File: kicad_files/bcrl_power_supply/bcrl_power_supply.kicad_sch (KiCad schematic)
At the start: 7 parts, among them J1 OSTVN02A150, J2 OSTVN02A150, J3 OSTVN02A150, J4 OSTVN02A150, J5 OSTVN02A150, J6 OSTVN02A150, J7 OSTVN02A150

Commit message: ...
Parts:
- added CJ2, PJ1: Conn_01x10, Connector_PinSocket_2.54mm:PinSocket_1x10_P2.54mm_Vertical, symbol Connector_Generic:Conn_01x10
- added P1: Conn_01x10, Connector_PinSocket_1.27mm:PinSocket_1x10_P1.27mm_Vertical, symbol Connector_Generic:Conn_01x10
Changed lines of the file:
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@@
+    )
+  )
+  (symbol (lib_id "Connector_Generic:Conn_01x10") (at 66.04 171.45 0) (unit 1)
+    (in_bom yes) (on_board yes) (dnp no) (fields_autoplaced)
+    (property "Reference" "P1" (at 68.58 171.45 0)
+      (effects (font (size 1.27 1.27)) (justify left))
+    )
+    (property "Value" "Conn_01x10" (at 68.58 173.99 0)
+      (effects (font (size 1.27 1.27)) (justify left))
+    )
+    (property "Footprint" "Connector_PinSocket_1.27mm:PinSocket_1x10_P1.27mm_Vertical" (at 66.04 171.45 0)
+      (effects (font (size 1.27 1.27)) hide)
+    )
+    (property "Datasheet" "~" (at 66.04 171.45 0)
+      (effects (font (size 1.27 1.27)) hide)
+    )
+    (pin "6")
+    (pin "9")
+    (pin "8")
+    (pin "5")
+    (pin "4")
+    (pin "3")
+    (pin "2")
+    (pin "10")
+    (pin "1")
+    (pin "7")
+    (instances
+      (project "bcrl_power_supply"
+        (path "/77f0f57c-9586-4625-9281-fa8cbd8015db"
+          (reference "P1") (unit 1)
+        )
+      )
     )
   )
@@
     )
   )
-  (symbol (lib_id "power:GND") (at 60.96 24.13 0) (unit 1)
-    (in_bom yes) (on_board yes) (dnp no) (fields_autoplaced)
-    (property "Reference" "#PWR02" (at 60.96 30.48 0)
-      (effects (font (size 1.27 1.27)) hide)
-    )
-    (property "Value" "GND" (at 60.96 29.21 0)
+  (symbol (lib_id "power:GND") (at 68.58 27.94 0) (unit 1)
+    (in_bom yes) (on_board yes) (dnp no) (fields_autoplaced)
+    (property "Reference" "#PWR02" (at 68.58 34.29 0)
+      (effects (font (size 1.27 1.27)) hide)
+    )
+    (property "Value" "GND" (at 68.58 33.02 0)
       (effects (font (size 1.27 1.27)))
     )
-    (property "Footprint" "" (at 60.96 24.13 0)
-      (effects (font (size 1.27 1.27)) hide)
-    )
-    (property "Datasheet" "" (at 60.96 24.13 0)
+    (property "Footprint" "" (at 68.58 27.94 0)
+      (effects (font (size 1.27 1.27)) hide)
+    )
+    (property "Datasheet" "" (at 68.58 27.94 0)
       (effects (font (size 1.27 1.27)) hide)
     )
@@
     )
   )
+  (symbol (lib_id "Connector_Generic:Conn_01x10") (at 67.31 128.27 0) (unit 1)
+    (in_bom yes) (on_board yes) (dnp no) (fields_autoplaced)
+    (property "Reference" "PJ1" (at 69.85 128.27 0)
+      (effects (font (size 1.27 1.27)) (justify left))
+    )
+    (property "Value" "Conn_01x10" (at 69.85 130.81 0)
+      (effects (font (size 1.27 1.27)) (justify left))
+    )
+    (property "Footprint" "Connector_PinSocket_2.54mm:PinSocket_1x10_P2.54mm_Vertical" (at 67.31 128.27 0)
+      (effects (font (size 1.27 1.27)) hide)
+    )
+    (property "Datasheet" "~" (at 67.31 128.27 0)
+      (effects (font (size 1.27 1.27)) hide)
+    )
+    (pin "6")
+    (pin "9")
+    (pin "8")
+    (pin "5")
+    (pin "4")
+    (pin "3")
+    (pin "2")
+    (pin "10")
+    (pin "1")
+    (pin "7")
+    (instances
+      (project "bcrl_power_supply"
+        (path "/77f0f57c-9586-4625-9281-fa8cbd8015db"
+          (reference "PJ1") (unit 1)
+        )
+      )
+    )
+  )
   (symbol (lib_id "2024-02-14_22-22-09:OSTVN02A150") (at 115.57 144.78 0) (unit 1)
     (in_bom yes) (on_board yes) (dnp no) (fields_autoplaced)
@@
         )
       )
+    )
+  )
+  (symbol (lib_id "Connector_Generic:Conn_01x10") (at 67.31 100.33 0) (unit 1)
+    (in_bom yes) (on_board yes) (dnp no) (fields_autoplaced)
+    (property "Reference" "CJ2" (at 69.85 100.33 0)
+      (effects (font (size 1.27 1.27)) (justify left))
+    )
+    (property "Value" "Conn_01x10" (at 69.85 102.87 0)
+      (effects (font (size 1.27 1.27)) (justify left))
+    )
+    (property "Footprint" "Connector_PinSocket_2.54mm:PinSocket_1x10_P2.54mm_Vertical" (at 67.31 100.33 0)
+      (effects (font (size 1.27 1.27)) hide)
+    )
+    (property "Datasheet" "~" (at 67.31 100.33 0)
+      (effects (font (size 1.27 1.27)) hide)
+    )
+    (pin "6")
+    (pin "9")
+    (pin "8")
+    (pin "5")
+    (pin "4")
+    (pin "3")
+    (pin "2")
+    (pin "10")
+    (pin "1")
+    (pin "7")
+    (instances
+      (project "bcrl_power_supply"
+        (path "/77f0f57c-9586-4625-9281-fa8cbd8015db"
+          (reference "CJ2") (unit 1)
+        )
+      )

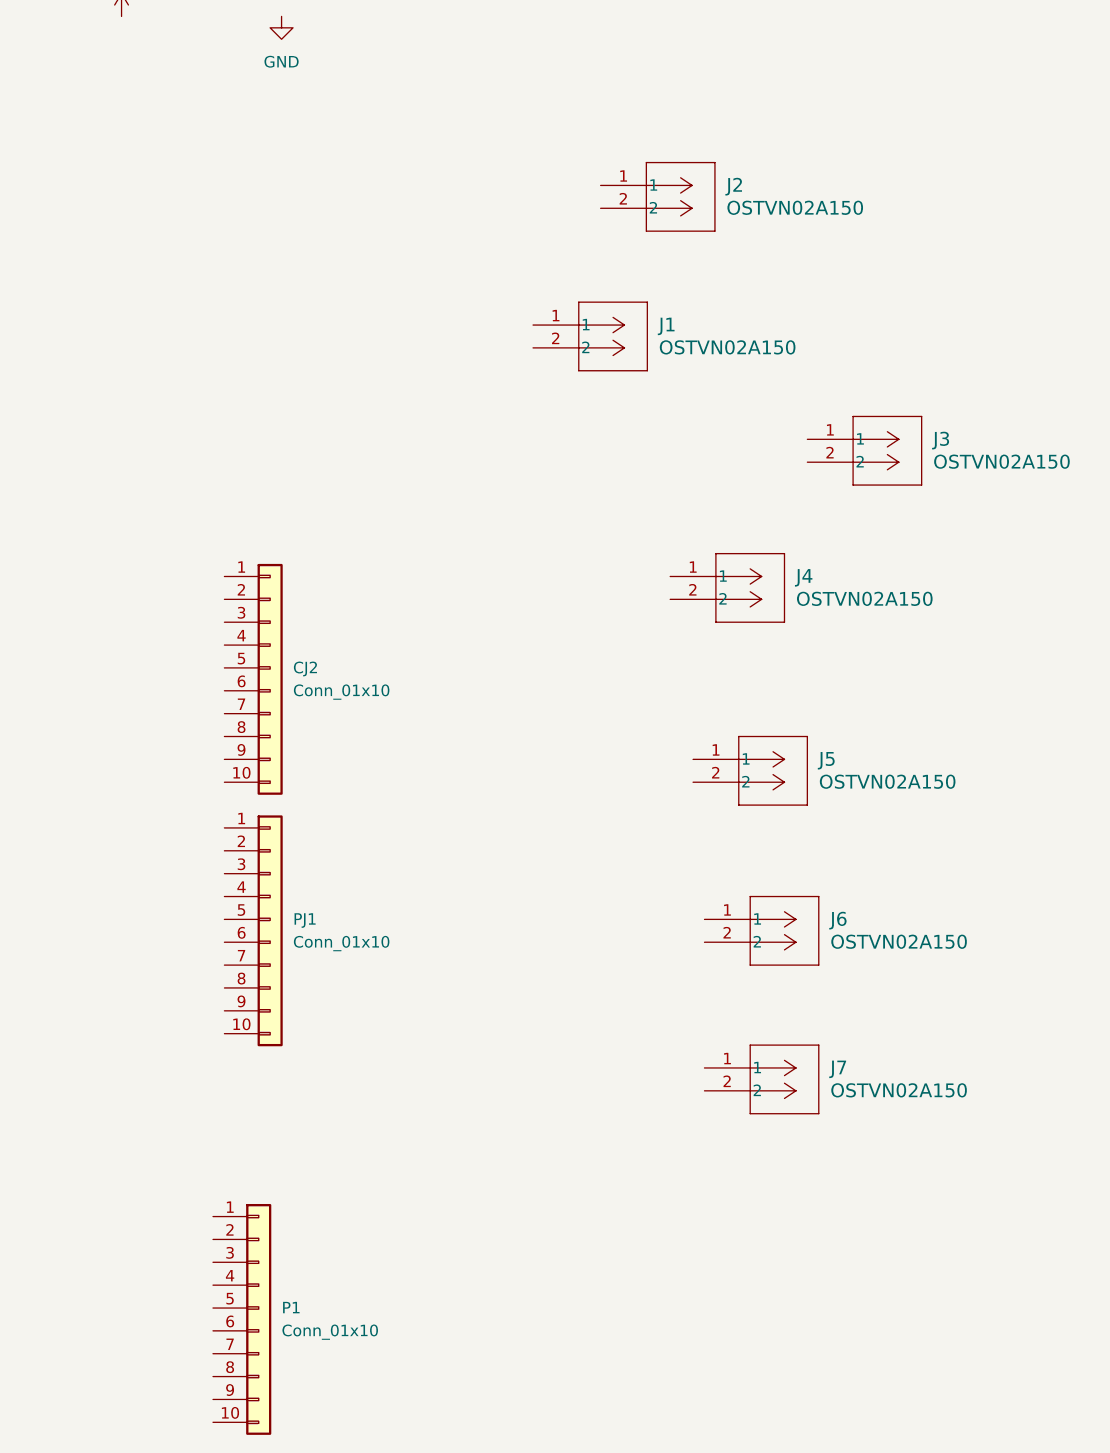
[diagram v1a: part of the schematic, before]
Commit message: added components
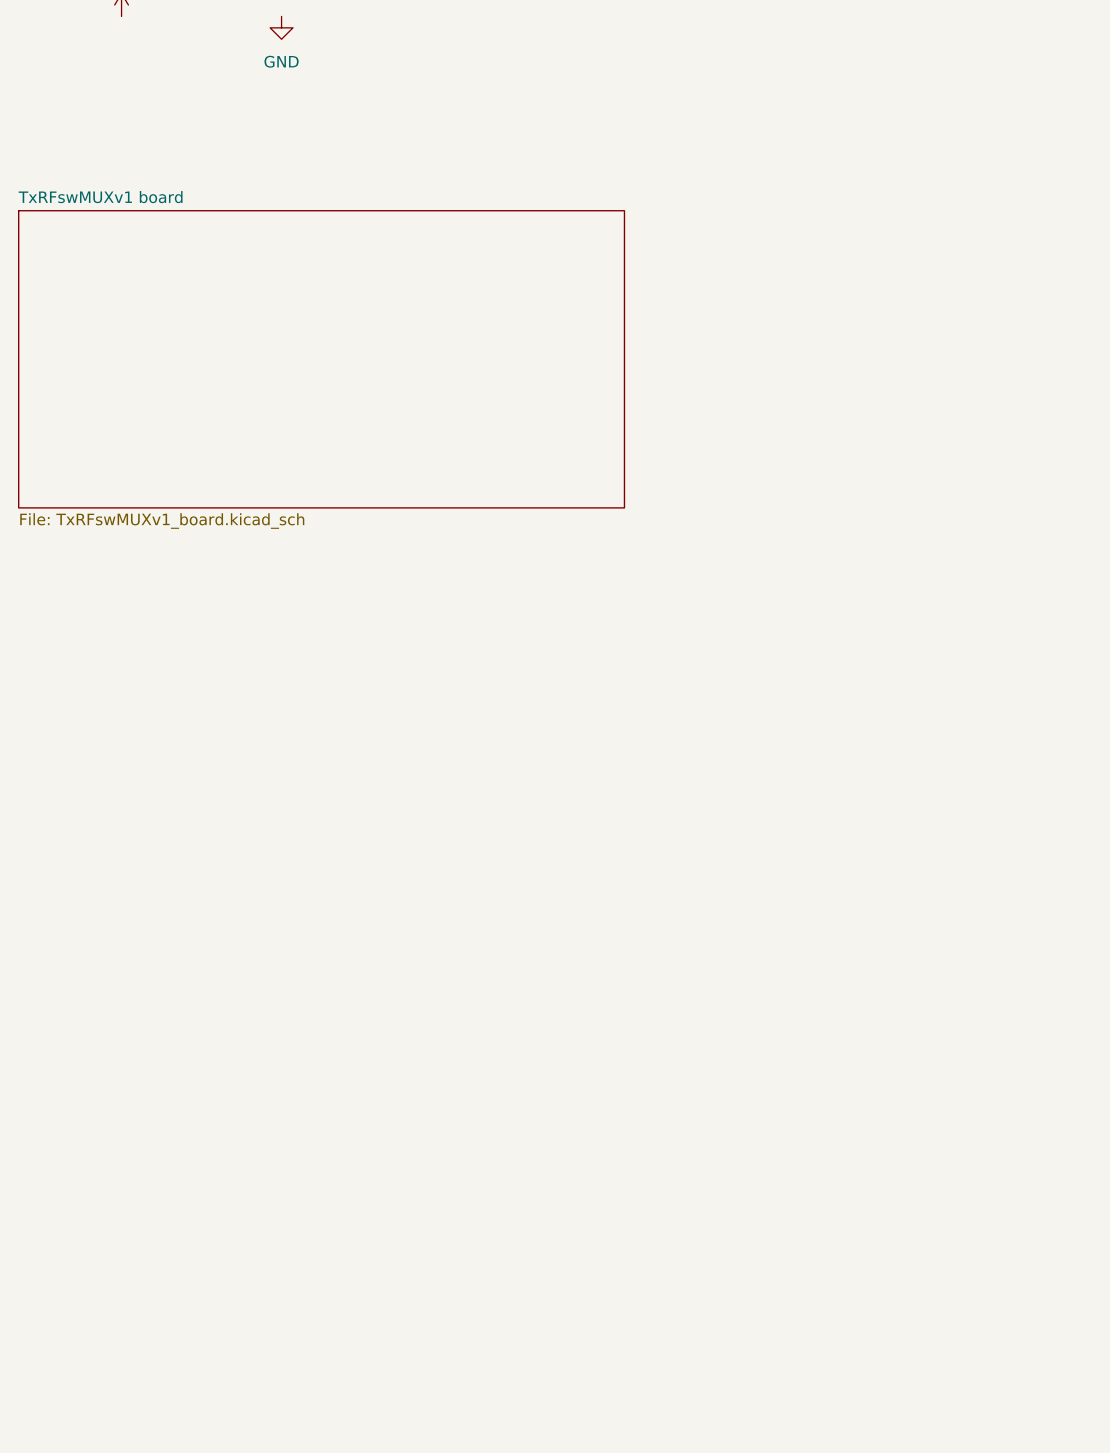
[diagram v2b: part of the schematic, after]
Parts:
- removed CJ2, PJ1: Conn_01x10, Connector_PinSocket_2.54mm:PinSocket_1x10_P2.54mm_Vertical, symbol Connector_Generic:Conn_01x10
- removed J1, J2, J3, J4, J5, J6, J7: OSTVN02A150, screw_terminal:CONN_OSTVN02A150_OST, symbol 2024-02-14_22-22-09:OSTVN02A150
- removed P1: Conn_01x10, Connector_PinSocket_1.27mm:PinSocket_1x10_P1.27mm_Vertical, symbol Connector_Generic:Conn_01x10
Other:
- added sheet TxRFswMUXv1 board (TxRFswMUXv1_board.kicad_sch)

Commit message: added decoupling
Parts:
- added J10, J12: OSTVN02A150, symbol BCRL_power_supply:OSTVN02A150
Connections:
- net +48V: now also J10.1, J12.1
- net GND: now also J10.2, J12.2
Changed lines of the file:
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@@
 (kicad_sch (version 20230121) (generator eeschema)
   (paper "A4")
-  (symbol (lib_id "power:+48V") (at 50.8 27.94 0) (unit 1)
+  (wire (pts (xy 30.48 34.29) (xy 39.37 34.29))
+    (stroke (width 0) (type default))
+  )
+  (wire (pts (xy 30.48 24.13) (xy 39.37 24.13))
+    (stroke (width 0) (type default))
+  )
+  (wire (pts (xy 30.48 36.83) (xy 39.37 36.83))
+    (stroke (width 0) (type default))
+  )
+  (wire (pts (xy 30.48 26.67) (xy 39.37 26.67))
+    (stroke (width 0) (type default))
+  )
+  (symbol (lib_id "BCRL_power_supply:OSTVN02A150") (at 39.37 34.29 0) (unit 1)
     (in_bom yes) (on_board yes) (dnp no) (fields_autoplaced)
-    (property "Reference" "#PWR01" (at 50.8 31.75 0)
+    (property "Reference" "J10" (at 53.34 34.29 0)
+      (effects (font (size 1.524 1.524)) (justify left))
+    )
+    (property "Value" "OSTVN02A150" (at 53.34 36.83 0)
+      (effects (font (size 1.524 1.524)) (justify left))
+    )
+    (property "Footprint" "" (at 29.21 29.21 0)
+      (effects (font (size 1.27 1.27) italic) hide)
+    )
+    (property "Datasheet" "" (at 33.02 31.75 0)
+      (effects (font (size 1.27 1.27) italic) hide)
+    )
+    (pin "1")
+    (pin "2")
+    (instances
+      (project "bcrl_power_supply"
+        (path "/77f0f57c-9586-4625-9281-fa8cbd8015db"
+          (reference "J10") (unit 1)
+        )
+      )
+    )
+  )
+  (symbol (lib_id "power:+48V") (at 30.48 24.13 90) (unit 1)
+    (in_bom yes) (on_board yes) (dnp no) (fields_autoplaced)
+    (property "Reference" "#PWR090" (at 34.29 24.13 0)
       (effects (font (size 1.27 1.27)) hide)
     )
-    (property "Value" "+48V" (at 50.8 22.86 0)
-      (effects (font (size 1.27 1.27)))
+    (property "Value" "+48V" (at 31.75 24.13 90)
+      (effects (font (size 1.27 1.27)) (justify right))
     )
-    (property "Footprint" "" (at 50.8 27.94 0)
+    (property "Footprint" "" (at 30.48 24.13 0)
       (effects (font (size 1.27 1.27)) hide)
     )
-    (property "Datasheet" "" (at 50.8 27.94 0)
+    (property "Datasheet" "" (at 30.48 24.13 0)
+      (effects (font (size 1.27 1.27)) hide)
+    )
+    (pin "1")
+    (instances
+      (project "bcrl_power_supply"
+        (path "/77f0f57c-9586-4625-9281-fa8cbd8015db"
+          (reference "#PWR090") (unit 1)
+        )
+      )
+    )
+  )
+  (symbol (lib_id "power:+48V") (at 30.48 34.29 90) (unit 1)
+    (in_bom yes) (on_board yes) (dnp no) (fields_autoplaced)
+    (property "Reference" "#PWR01" (at 34.29 34.29 0)
+      (effects (font (size 1.27 1.27)) hide)
+    )
+    (property "Value" "+48V" (at 31.75 34.29 90)
+      (effects (font (size 1.27 1.27)) (justify right))
+    )
+    (property "Footprint" "" (at 30.48 34.29 0)
+      (effects (font (size 1.27 1.27)) hide)
+    )
+    (property "Datasheet" "" (at 30.48 34.29 0)
       (effects (font (size 1.27 1.27)) hide)
     )
@@
     )
   )
-  (symbol (lib_id "power:GND") (at 68.58 27.94 0) (unit 1)
+  (symbol (lib_id "power:GND") (at 30.48 26.67 270) (unit 1)
     (in_bom yes) (on_board yes) (dnp no) (fields_autoplaced)
-    (property "Reference" "#PWR02" (at 68.58 34.29 0)
+    (property "Reference" "#PWR091" (at 24.13 26.67 0)
       (effects (font (size 1.27 1.27)) hide)
     )
-    (property "Value" "GND" (at 68.58 33.02 0)
-      (effects (font (size 1.27 1.27)))
+    (property "Value" "GND" (at 31.75 26.67 90)
+      (effects (font (size 1.27 1.27)) (justify left))
     )
-    (property "Footprint" "" (at 68.58 27.94 0)
+    (property "Footprint" "" (at 30.48 26.67 0)
       (effects (font (size 1.27 1.27)) hide)
     )
-    (property "Datasheet" "" (at 68.58 27.94 0)
+    (property "Datasheet" "" (at 30.48 26.67 0)
+      (effects (font (size 1.27 1.27)) hide)
+    )
+    (pin "1")
+    (instances
+      (project "bcrl_power_supply"
+        (path "/77f0f57c-9586-4625-9281-fa8cbd8015db"
+          (reference "#PWR091") (unit 1)
+        )
+      )
+    )
+  )
+  (symbol (lib_id "power:GND") (at 30.48 36.83 270) (unit 1)
+    (in_bom yes) (on_board yes) (dnp no) (fields_autoplaced)
+    (property "Reference" "#PWR02" (at 24.13 36.83 0)
+      (effects (font (size 1.27 1.27)) hide)
+    )
+    (property "Value" "GND" (at 31.75 36.83 90)
+      (effects (font (size 1.27 1.27)) (justify left))
+    )
+    (property "Footprint" "" (at 30.48 36.83 0)
+      (effects (font (size 1.27 1.27)) hide)
+    )
+    (property "Datasheet" "" (at 30.48 36.83 0)
       (effects (font (size 1.27 1.27)) hide)
     )
@@
         )
       )
+    )
+  )
+  (symbol (lib_id "BCRL_power_supply:OSTVN02A150") (at 39.37 24.13 0) (unit 1)
+    (in_bom yes) (on_board yes) (dnp no) (fields_autoplaced)
+    (property "Reference" "J12" (at 53.34 24.13 0)
+      (effects (font (size 1.524 1.524)) (justify left))
+    )
+    (property "Value" "OSTVN02A150" (at 53.34 26.67 0)
+      (effects (font (size 1.524 1.524)) (justify left))
+    )
+    (property "Footprint" "" (at 29.21 19.05 0)
+      (effects (font (size 1.27 1.27) italic) hide)
+    )
+    (property "Datasheet" "" (at 33.02 21.59 0)
+      (effects (font (size 1.27 1.27) italic) hide)
+    )
+    (pin "1")
+    (pin "2")
+    (instances
+      (project "bcrl_power_supply"
+        (path "/77f0f57c-9586-4625-9281-fa8cbd8015db"
+          (reference "J12") (unit 1)
+        )
+      )

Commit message: added EMC
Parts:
- renumbered J12 to J1, J10 to J2
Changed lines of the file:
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@@
   (symbol (lib_id "BCRL_power_supply:OSTVN02A150") (at 39.37 34.29 0) (unit 1)
     (in_bom yes) (on_board yes) (dnp no) (fields_autoplaced)
-    (property "Reference" "J10" (at 53.34 34.29 0)
+    (property "Reference" "J2" (at 53.34 34.29 0)
       (effects (font (size 1.524 1.524)) (justify left))
     )
@@
       (project "bcrl_power_supply"
         (path "/77f0f57c-9586-4625-9281-fa8cbd8015db"
-          (reference "J10") (unit 1)
+          (reference "J2") (unit 1)
         )
       )
@@
   (symbol (lib_id "power:+48V") (at 30.48 24.13 90) (unit 1)
     (in_bom yes) (on_board yes) (dnp no) (fields_autoplaced)
-    (property "Reference" "#PWR090" (at 34.29 24.13 0)
+    (property "Reference" "#PWR01" (at 34.29 24.13 0)
       (effects (font (size 1.27 1.27)) hide)
     )
@@
       (project "bcrl_power_supply"
         (path "/77f0f57c-9586-4625-9281-fa8cbd8015db"
-          (reference "#PWR090") (unit 1)
+          (reference "#PWR01") (unit 1)
         )
       )
@@
   (symbol (lib_id "power:+48V") (at 30.48 34.29 90) (unit 1)
     (in_bom yes) (on_board yes) (dnp no) (fields_autoplaced)
-    (property "Reference" "#PWR01" (at 34.29 34.29 0)
+    (property "Reference" "#PWR03" (at 34.29 34.29 0)
       (effects (font (size 1.27 1.27)) hide)
     )
@@
       (project "bcrl_power_supply"
         (path "/77f0f57c-9586-4625-9281-fa8cbd8015db"
-          (reference "#PWR01") (unit 1)
+          (reference "#PWR03") (unit 1)
         )
       )
@@
   (symbol (lib_id "power:GND") (at 30.48 26.67 270) (unit 1)
     (in_bom yes) (on_board yes) (dnp no) (fields_autoplaced)
-    (property "Reference" "#PWR091" (at 24.13 26.67 0)
+    (property "Reference" "#PWR02" (at 24.13 26.67 0)
       (effects (font (size 1.27 1.27)) hide)
     )
@@
       (project "bcrl_power_supply"
         (path "/77f0f57c-9586-4625-9281-fa8cbd8015db"
-          (reference "#PWR091") (unit 1)
+          (reference "#PWR02") (unit 1)
         )
       )
@@
   (symbol (lib_id "power:GND") (at 30.48 36.83 270) (unit 1)
     (in_bom yes) (on_board yes) (dnp no) (fields_autoplaced)
-    (property "Reference" "#PWR02" (at 24.13 36.83 0)
+    (property "Reference" "#PWR04" (at 24.13 36.83 0)
       (effects (font (size 1.27 1.27)) hide)
     )
@@
       (project "bcrl_power_supply"
         (path "/77f0f57c-9586-4625-9281-fa8cbd8015db"
-          (reference "#PWR02") (unit 1)
+          (reference "#PWR04") (unit 1)
         )
       )
@@
   (symbol (lib_id "BCRL_power_supply:OSTVN02A150") (at 39.37 24.13 0) (unit 1)
     (in_bom yes) (on_board yes) (dnp no) (fields_autoplaced)
-    (property "Reference" "J12" (at 53.34 24.13 0)
+    (property "Reference" "J1" (at 53.34 24.13 0)
       (effects (font (size 1.524 1.524)) (justify left))
     )
@@
       (project "bcrl_power_supply"
         (path "/77f0f57c-9586-4625-9281-fa8cbd8015db"
-          (reference "J12") (unit 1)
+          (reference "J1") (unit 1)
         )
       )

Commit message: added more circuits
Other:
- added sheet RxBFN-16C (BFN_board.kicad_sch)
- added sheet RxBFN-16C1 (BFN_board.kicad_sch)
- added sheet RxBFN-16C2 (BFN_board.kicad_sch)
- added sheet RxBFN-16C3 (BFN_board.kicad_sch)
- added sheet RxBFN-16F (BFN_board.kicad_sch)
- added sheet RxBFN-16F1 (BFN_board.kicad_sch)
- added sheet RxBFN-16F2 (BFN_board.kicad_sch)
- added sheet RxBFN-16F3 (BFN_board.kicad_sch)
- added sheet RxRFswMUXv1 board (RxRFswMUXv1_board.kicad_sch)
- added sheet Rx_AGC (AGC_board.kicad_sch)
- added sheet Tx RPi4 HAT board (RPi4_HAT_board.kicad_sch)
- added sheet TxBFN-16C (BFN_board.kicad_sch)
- added sheet TxBFN-16C1 (BFN_board.kicad_sch)
- added sheet TxBFN-16C2 (BFN_board.kicad_sch)
- added sheet TxBFN-16C3 (BFN_board.kicad_sch)
- added sheet TxBFN-16F (BFN_board.kicad_sch)
- added sheet TxBFN-16F1 (BFN_board.kicad_sch)
- added sheet TxBFN-16F2 (BFN_board.kicad_sch)
- added sheet TxBFN-16F3 (BFN_board.kicad_sch)
- added sheet Tx_AGC (AGC_board.kicad_sch)

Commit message: WIP
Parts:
- added J12: Conn_01x02, symbol Connector_Generic:Conn_01x02
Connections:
- net GND: now also J12.2 (Pin_2)
- new net EN_3.3V_FROM_5V: J12.1 (Pin_1)
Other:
- removed sheet RxBFN-16C1
- removed sheet RxBFN-16C2
- removed sheet RxBFN-16C3
- removed sheet RxBFN-16F1
- removed sheet RxBFN-16F2
- removed sheet RxBFN-16F3
- removed sheet TxBFN-16C1
- removed sheet TxBFN-16C2
- removed sheet TxBFN-16C3
- removed sheet TxBFN-16F1
- removed sheet TxBFN-16F2
- removed sheet TxBFN-16F3
- added sheet PDQ10-Q48-S3-D_EMC_1 (PDQ10-Q48-S3-D_EMC.kicad_sch)
- added sheet Tx RPi4 HAT board1 (RPi4_HAT_board.kicad_sch)

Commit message: cleanup PCB
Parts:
- added H1, H2, H3, H4: MountingHole, MountingHole:MountingHole_3.5mm_Pad, symbol Mechanical:MountingHole
- J1, J2: footprint (none) -> BCRL_power_supply:CONN_OSTVN02A150_OST
- J3: renamed from J12; footprint (none) -> Connector_PinHeader_2.54mm:PinHeader_1x02_P2.54mm_Vertical
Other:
- sheet Tx RPi4 HAT board renamed Tx_RPi4_HAT_board
- sheet Tx RPi4 HAT board1 renamed Rx_RPi4_HAT_board
- moved on the sheet: J3

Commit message: ...
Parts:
- added H5, H6: MountingHole, MountingHole:MountingHole_3.5mm_Pad, symbol Mechanical:MountingHole
- added J12: 5034801600, BCRL_power_supply:MOLEX_5034801600, symbol BCRL_power_supply:5034801600
- renumbered H2 to H1, H1 to H2
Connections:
- net GND: now also J12.S1 (SHIELD), J12.S2 (SHIELD__1)
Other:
- added sheet Rx_Eth_Switch (Eth_Switch.kicad_sch)
- added sheet Tx_Eth_Switch (Eth_Switch.kicad_sch)
- moved on the sheet: H1, H2, H3, H4, J3
